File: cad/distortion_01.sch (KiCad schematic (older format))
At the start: 105 parts, among them CON101 Ext_PSU, J101 JACK_IN, J102 JACK_OUT, P101 Battery_conn, P102 BYPASS_SWITCH, P103 CONN_01X03, P104 CONN_01X03, P105 CONN_01X03, P106 CONN_01X03, Q101 BS170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

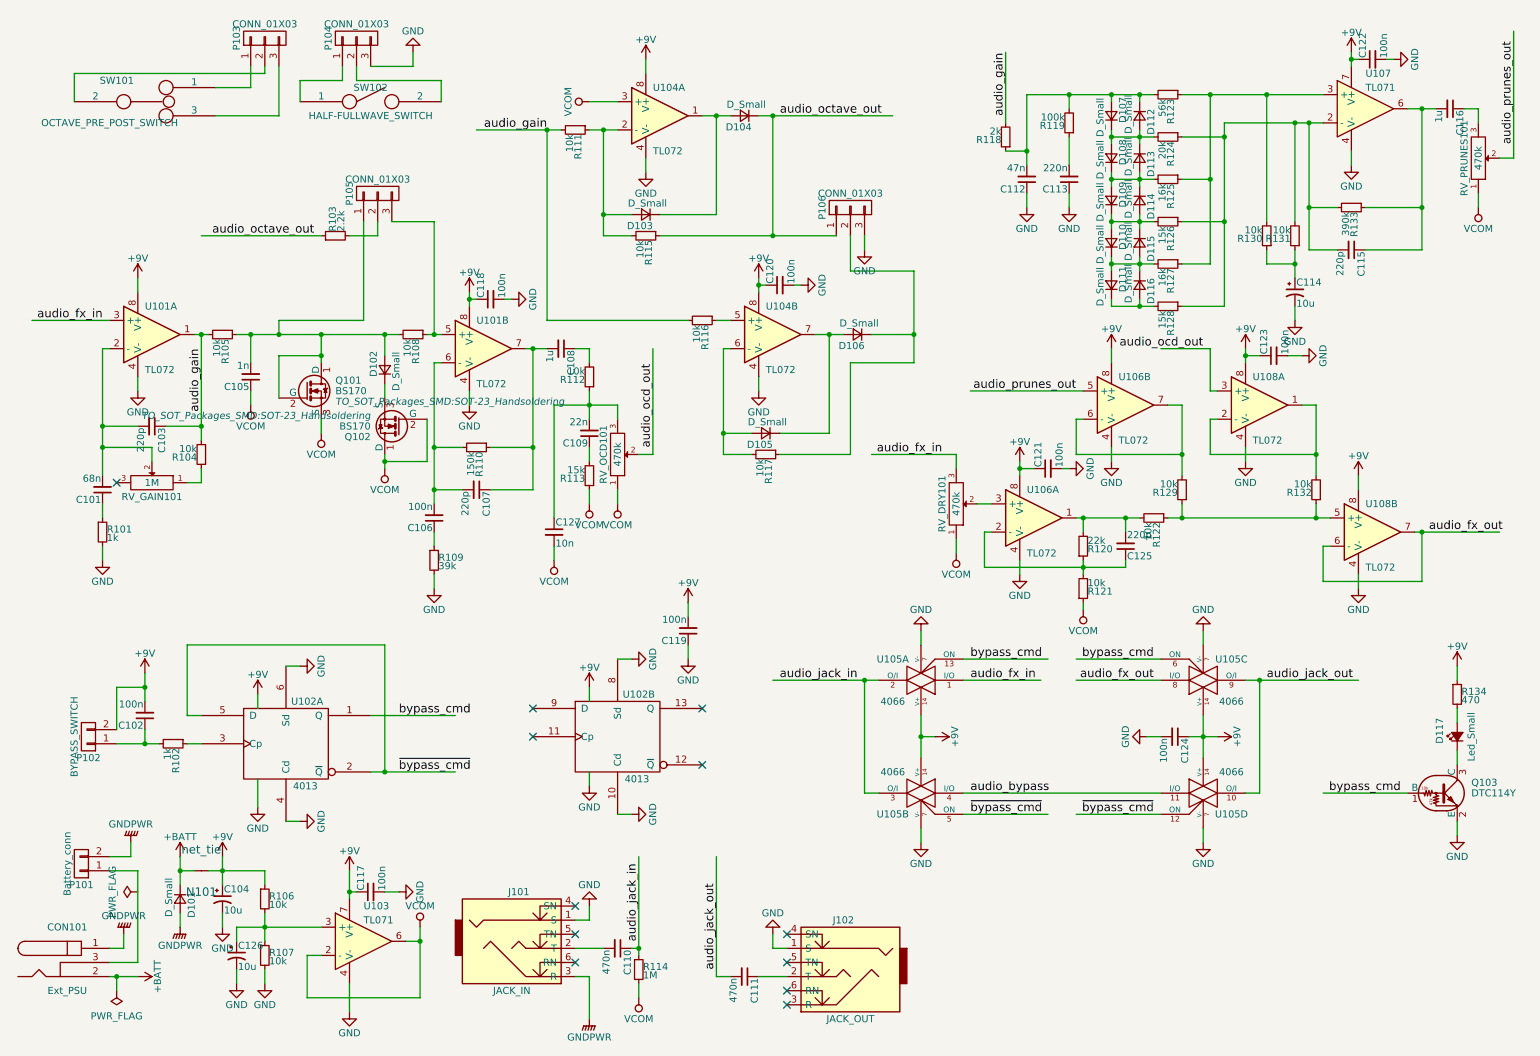
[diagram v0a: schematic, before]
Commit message: Corrected pots polarity (schematic and layout).
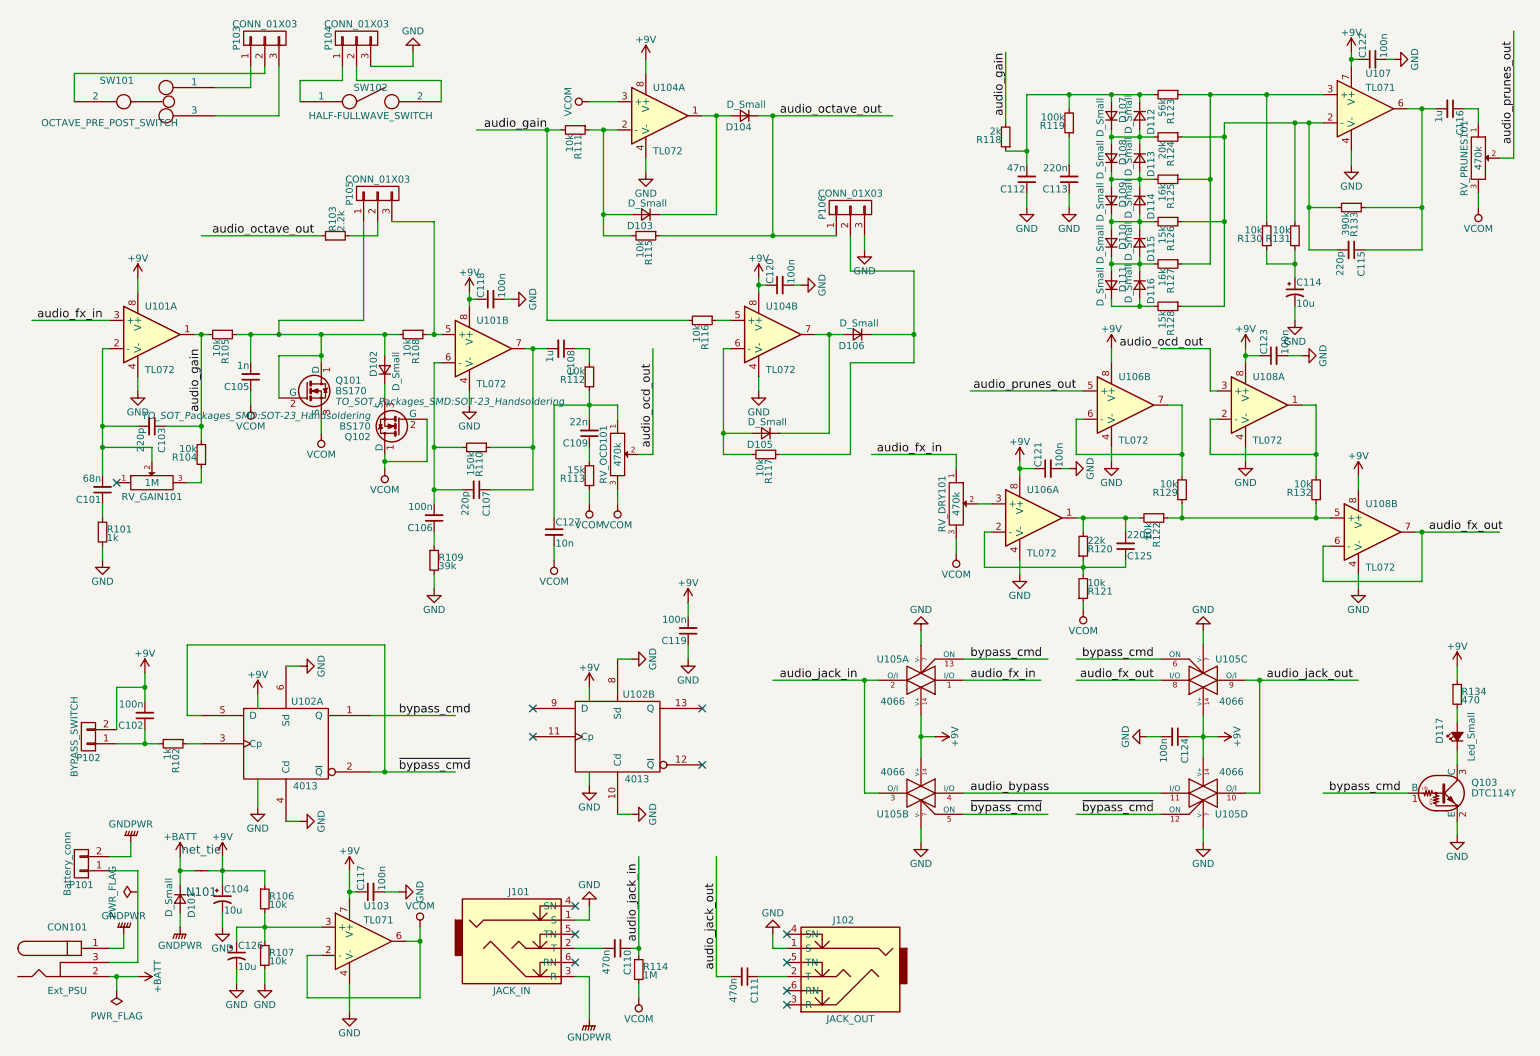
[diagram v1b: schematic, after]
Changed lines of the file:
@@
 F 3 "" H 1500 3750 50  0000 C CNN
 	1    1500 3750
-	-1   0    0    -1
+	1    0    0    -1
 $EndComp
 NoConn ~ 1250 3750
@@
 F 3 "" H 4800 3550 50  0000 C CNN
 	1    4800 3550
-	0    1    -1   0
+	0    1    1    0
 $EndComp
 $Comp
@@
 F 3 "" H 10900 1450 50  0000 C CNN
 	1    10900 1450
-	0    1    -1   0
+	0    1    1    0
 $EndComp
 $Comp
@@
 F 3 "" H 7200 3900 50  0000 C CNN
 	1    7200 3900
-	0    1    -1   0
-$EndComp
-$Comp
+	0    1    1    0
+$EndComp
+$Comp

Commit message: Added schematics screenshots.
Changed diodes symbols to BAS21.
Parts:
- removed D107, D108, D109, D110, D111, D112, D113, D114, D115, D116: D_Small, TO_SOT_Packages_SMD:SOT-23_Handsoldering, symbol D_Small
- added D107, D108, D109, D110, D111, D112, D113, D114, D115, D116: BAS21, TO_SOT_Packages_SMD:SOT-23, symbol BAS21
- Q101, Q102: symbol BS170 -> BS170-RESCUE-distortion_01
- U103, U107: symbol TL071 -> TL071-RESCUE-distortion_01
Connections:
- wire segments 308 -> 310
- no-connect marks 12 -> 14
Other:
- moved on the sheet: R123, R124, R125, R126, R127, R128

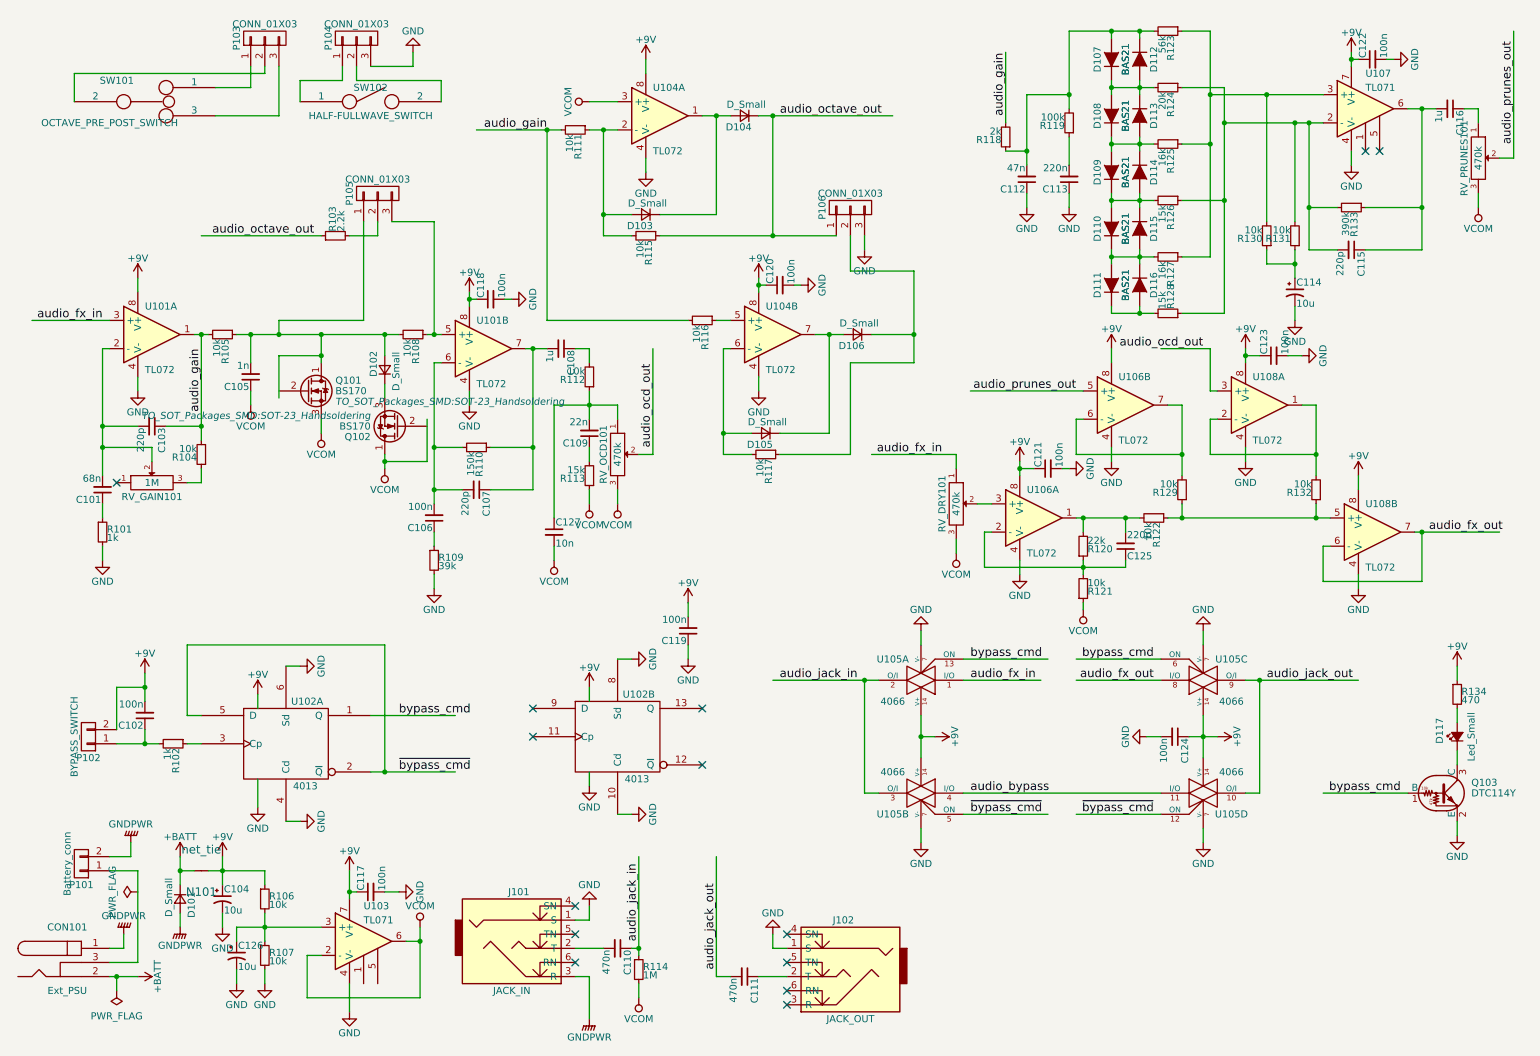
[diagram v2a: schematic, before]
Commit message: Added output capacitor on Prunes.
Changed capacitor value on octave output.
Corrected layout accordingly.
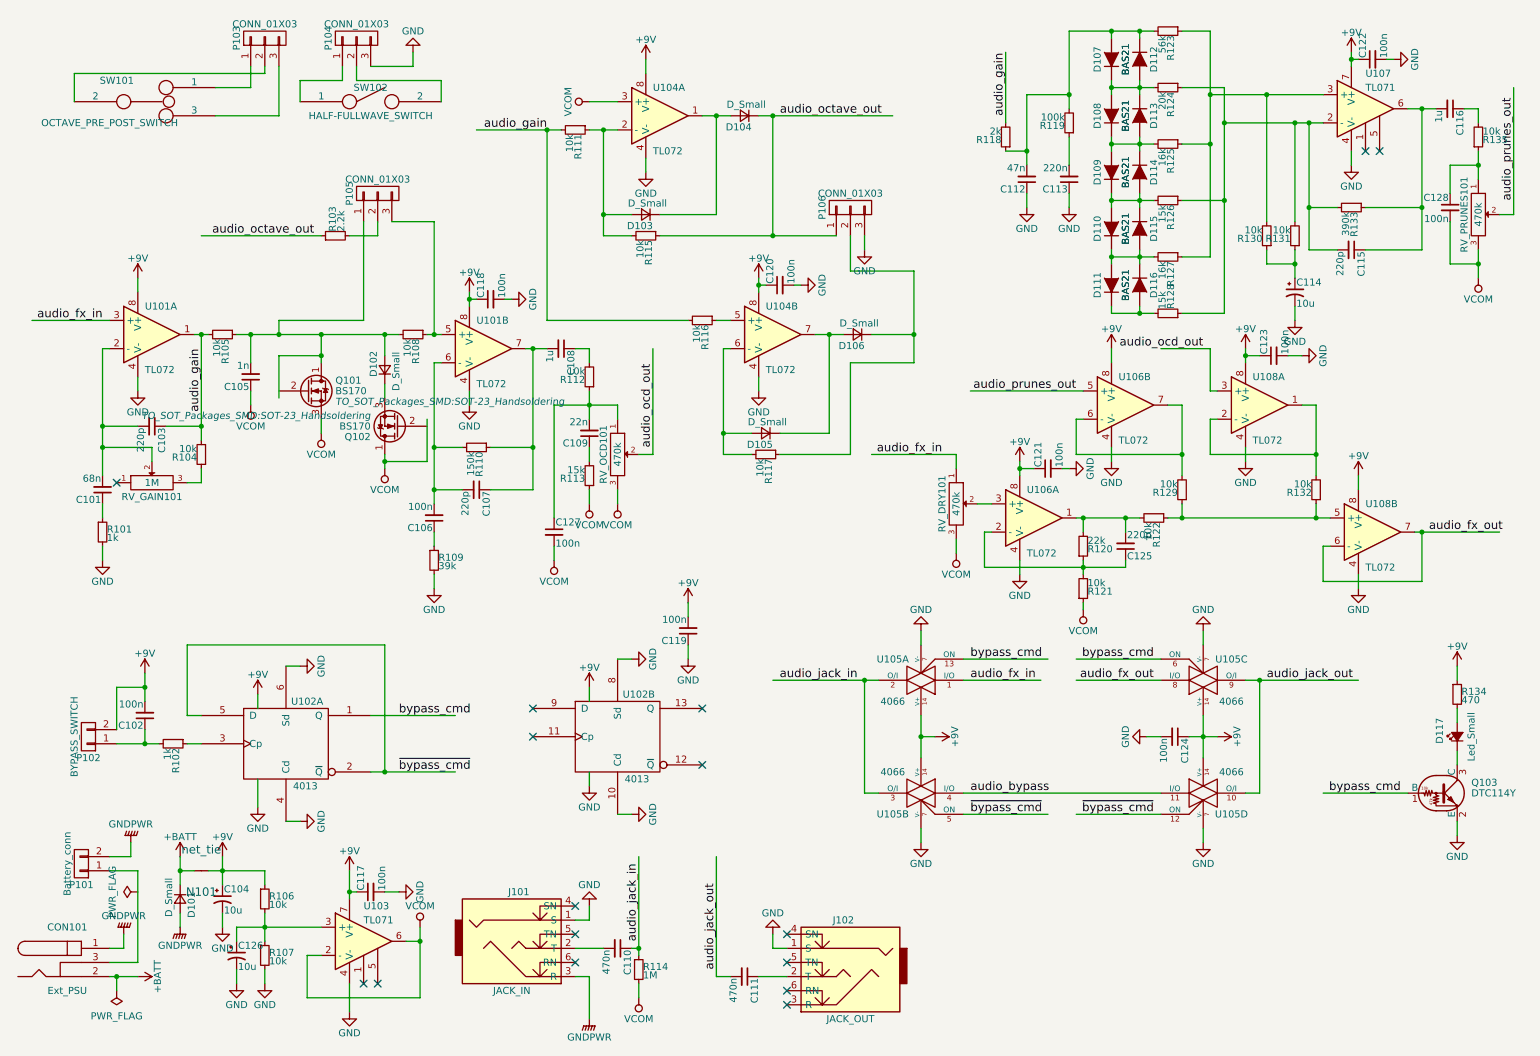
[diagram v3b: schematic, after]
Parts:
- added C128: 100n, Capacitors_SMD:C_0603_HandSoldering, symbol C_Small
- added R135: 10k, Resistors_SMD:R_0603_HandSoldering, symbol R_Small
- C127: value 10n -> 100n
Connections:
- wire segments 310 -> 315
- no-connect marks 14 -> 16
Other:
- moved on the sheet: RV_PRUNES101
